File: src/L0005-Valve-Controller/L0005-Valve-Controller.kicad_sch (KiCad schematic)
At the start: 62 parts, among them J1 Jumper_NO, J2 Jumper_NO, P1 3220-20-0200-00, P10 353620650, P11 353620650, P12 353620650, P13 353620650, P14 647676-3, P15 647676-3, P16 647676-2, P2 140-504-415-000, P9 647676-2, U1 LPC54113J256BD64QL, U2 LMS8117AMP-3.3_NOPB, U3 MAX3370EXK+T, U4 MAX3370EXK+T, U5 Optocoupler

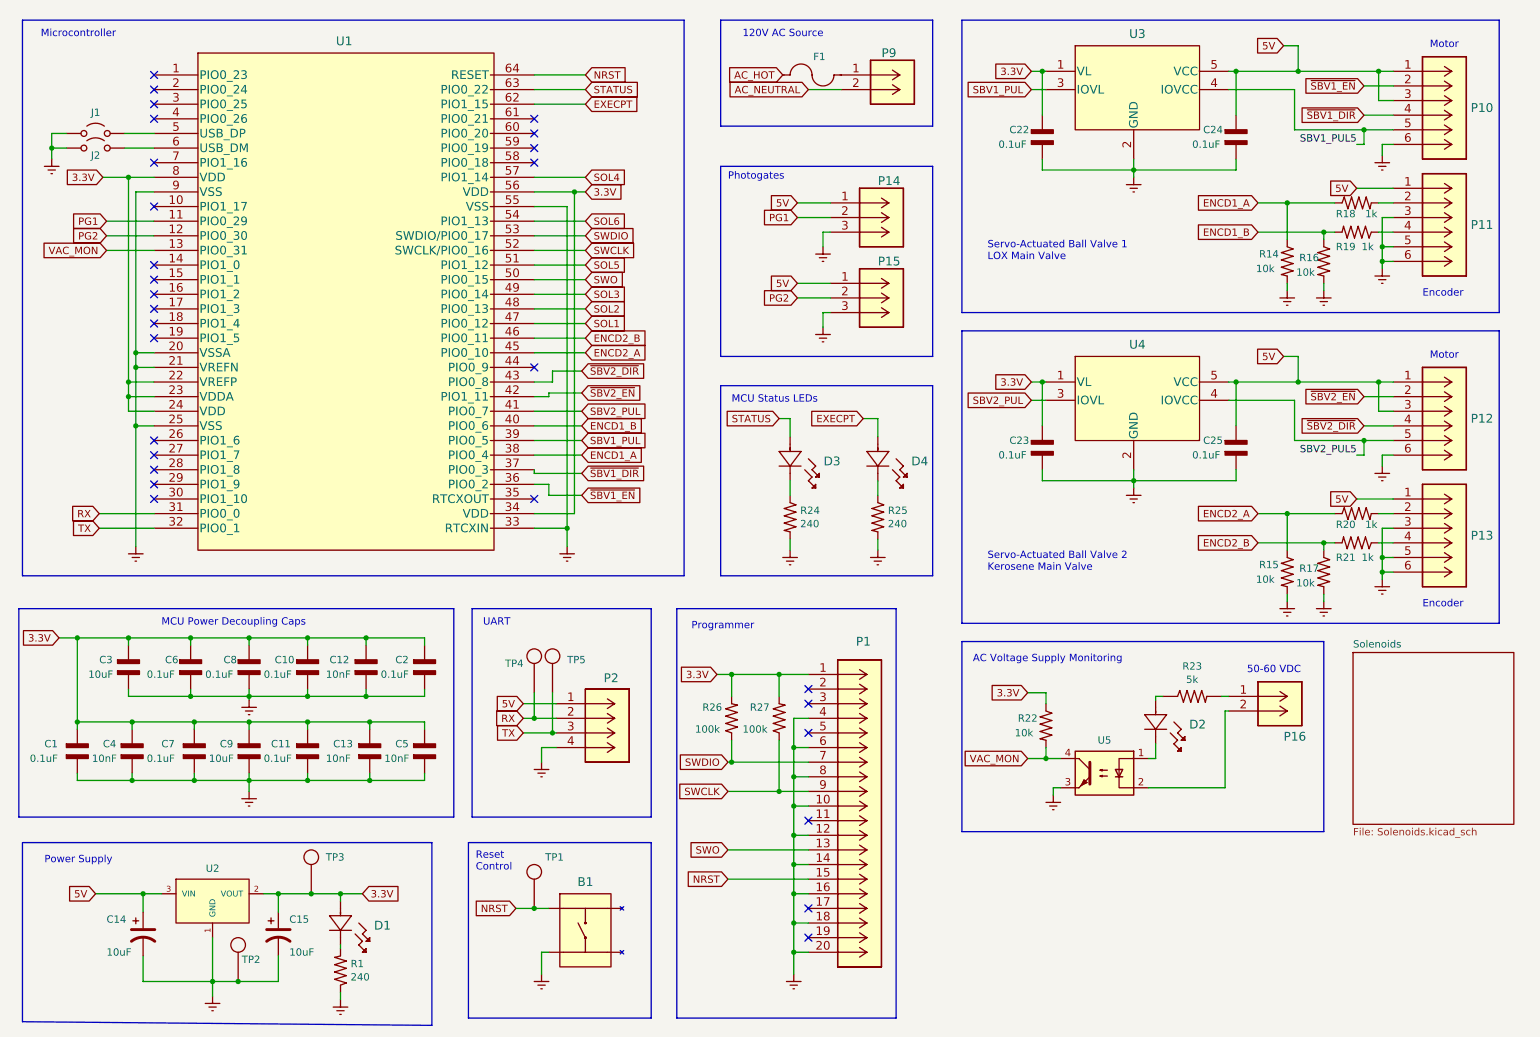
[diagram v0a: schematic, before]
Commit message: moved stepper circuits to second schematic sheet
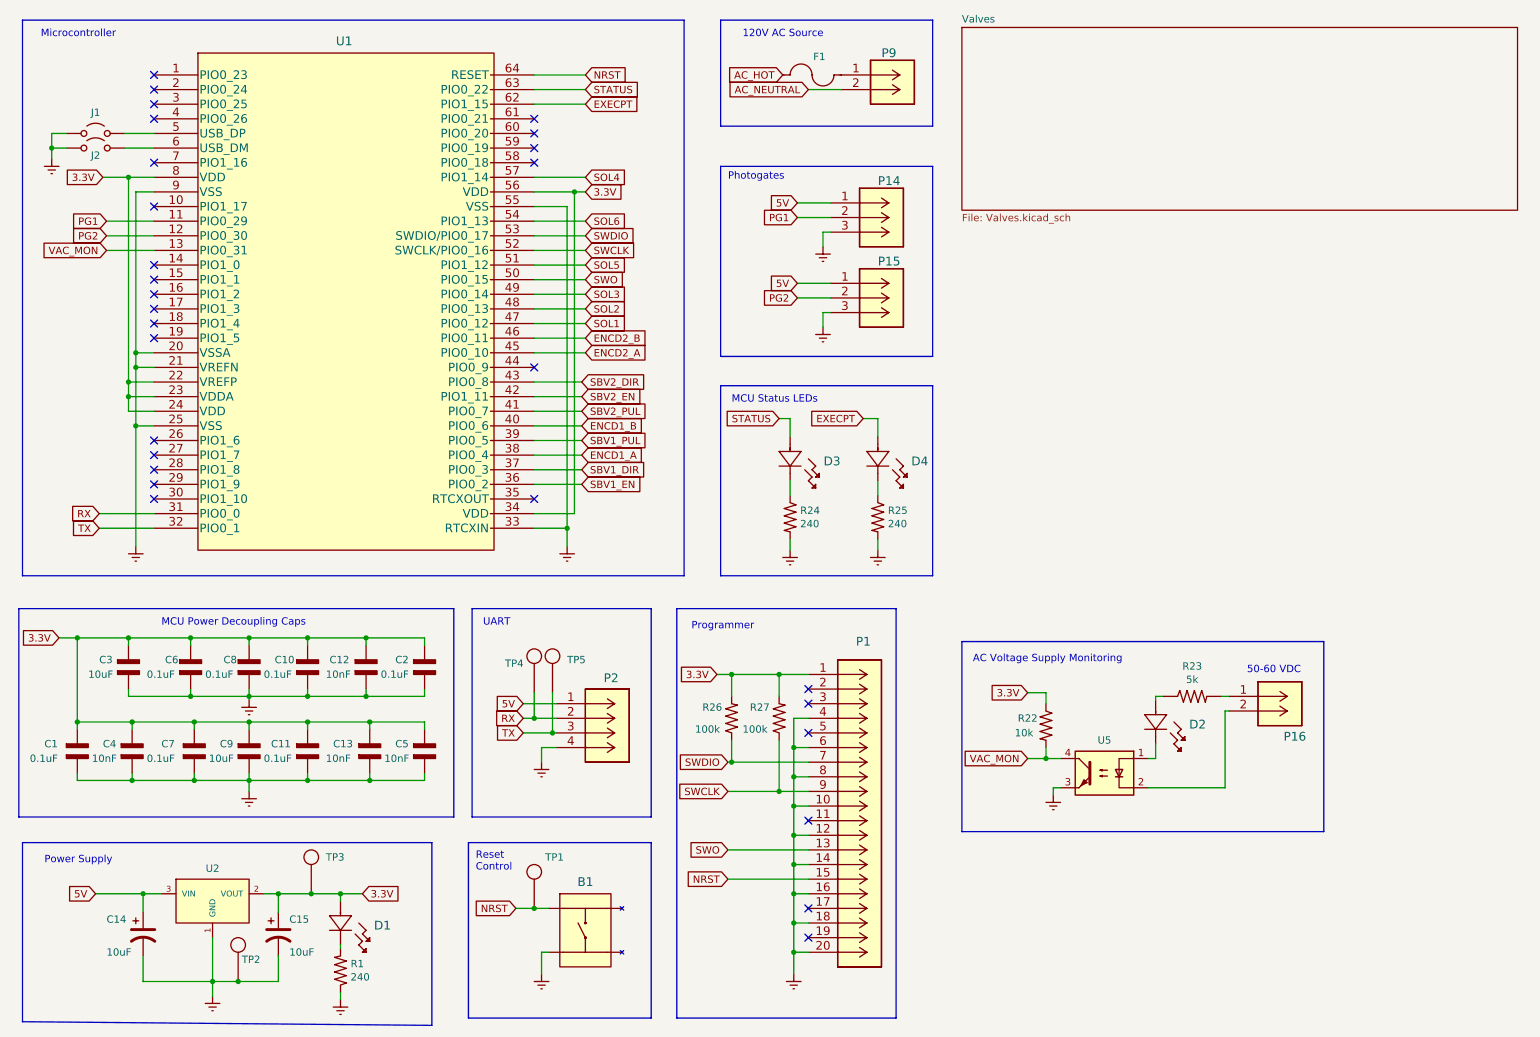
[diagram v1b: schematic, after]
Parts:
- removed C22, C23, C24, C25: 0.1uF, L0005-Valve-Controller:CAP_0603, symbol L0005-Valve-Controller:CAP_0603
- removed P10, P11, P12, P13: 353620650, L0005-Valve-Controller:MOLEX_35362-0650, symbol L0005-Valve-Controller:353620650
- removed R14, R15, R16, R17: 10k, L0005-Valve-Controller:RES_0603, symbol L0005-Valve-Controller:RES_0603
- removed R18, R19, R20, R21: 1k, L0005-Valve-Controller:RES_0603, symbol L0005-Valve-Controller:RES_0603
- removed U3, U4: MAX3370EXK+T, L0005-Valve-Controller:MAX3370EXK&plus_T, symbol L0005-Valve-Controller:MAX3370EXK+T
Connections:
- net ~{SBV1_DIR} renamed SBV1_DIR
- net ~{SBV1_EN} renamed SBV1_EN
- net ~{SBV2_DIR} renamed SBV2_DIR
- net ~{SBV2_EN} renamed SBV2_EN
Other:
- sheet Solenoids renamed Valves
- sheet Valves: file Solenoids.kicad_sch -> Valves.kicad_sch
- note removed: "Encoder"
- note removed: "Motor"
- note removed: "Servo-Actuated Ball Valve 1 LOX Main Valve"
- note removed: "Servo-Actuated Ball Valve 2 Kerosene Main Valve"

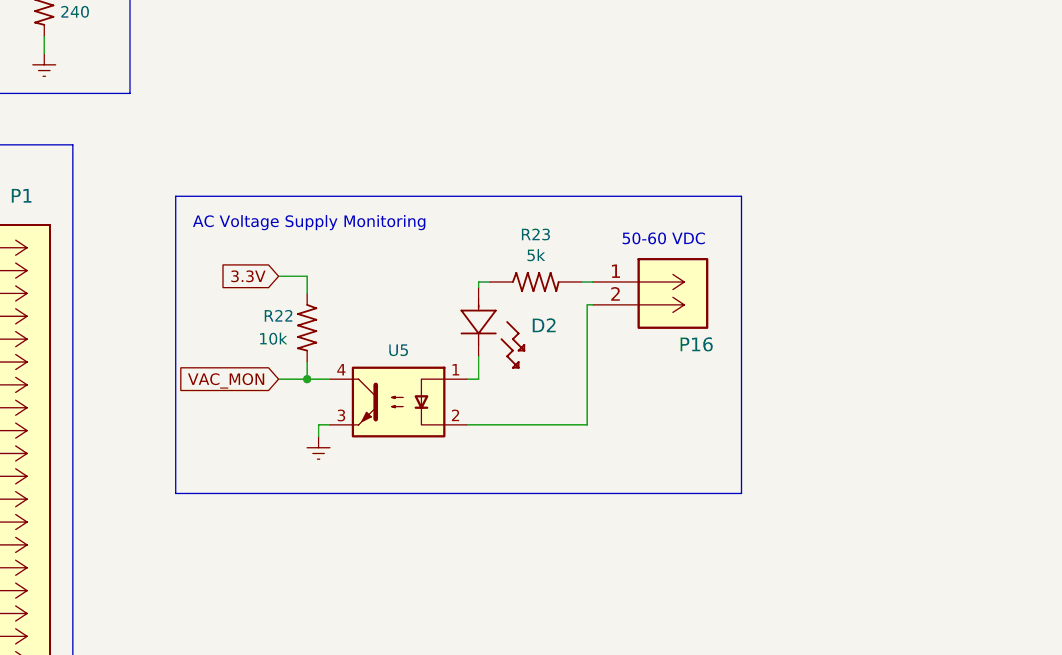
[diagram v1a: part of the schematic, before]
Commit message: inverted VAC_MON signal
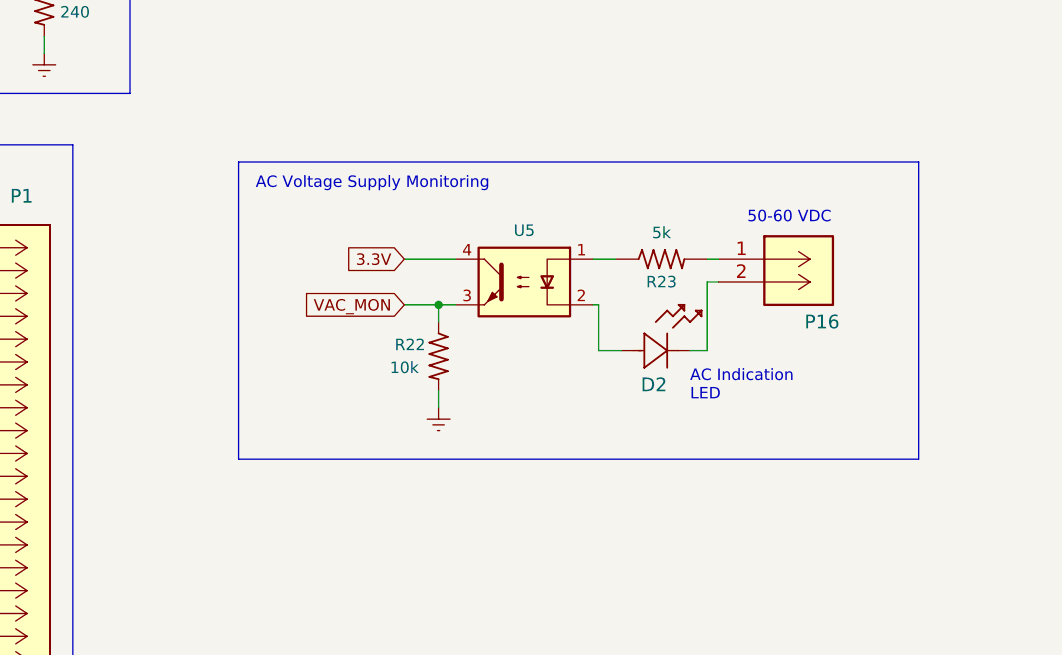
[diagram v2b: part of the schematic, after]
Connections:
- net 3.3V: now also U5.4; no longer R22.1
- net Earth: now also R22.2; no longer U5.3
- net VAC_MON: now also R22.1, U5.3; no longer R22.2, U5.4
- net at P16.2: now also D2.1; no longer U5.2
- net at U5.1: now also R23.1; no longer D2.1
- net at D2.2: now also U5.2; no longer R23.1
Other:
- note added: "AC Indication LED"
- moved on the sheet: D2, P16, R22, R23, U5

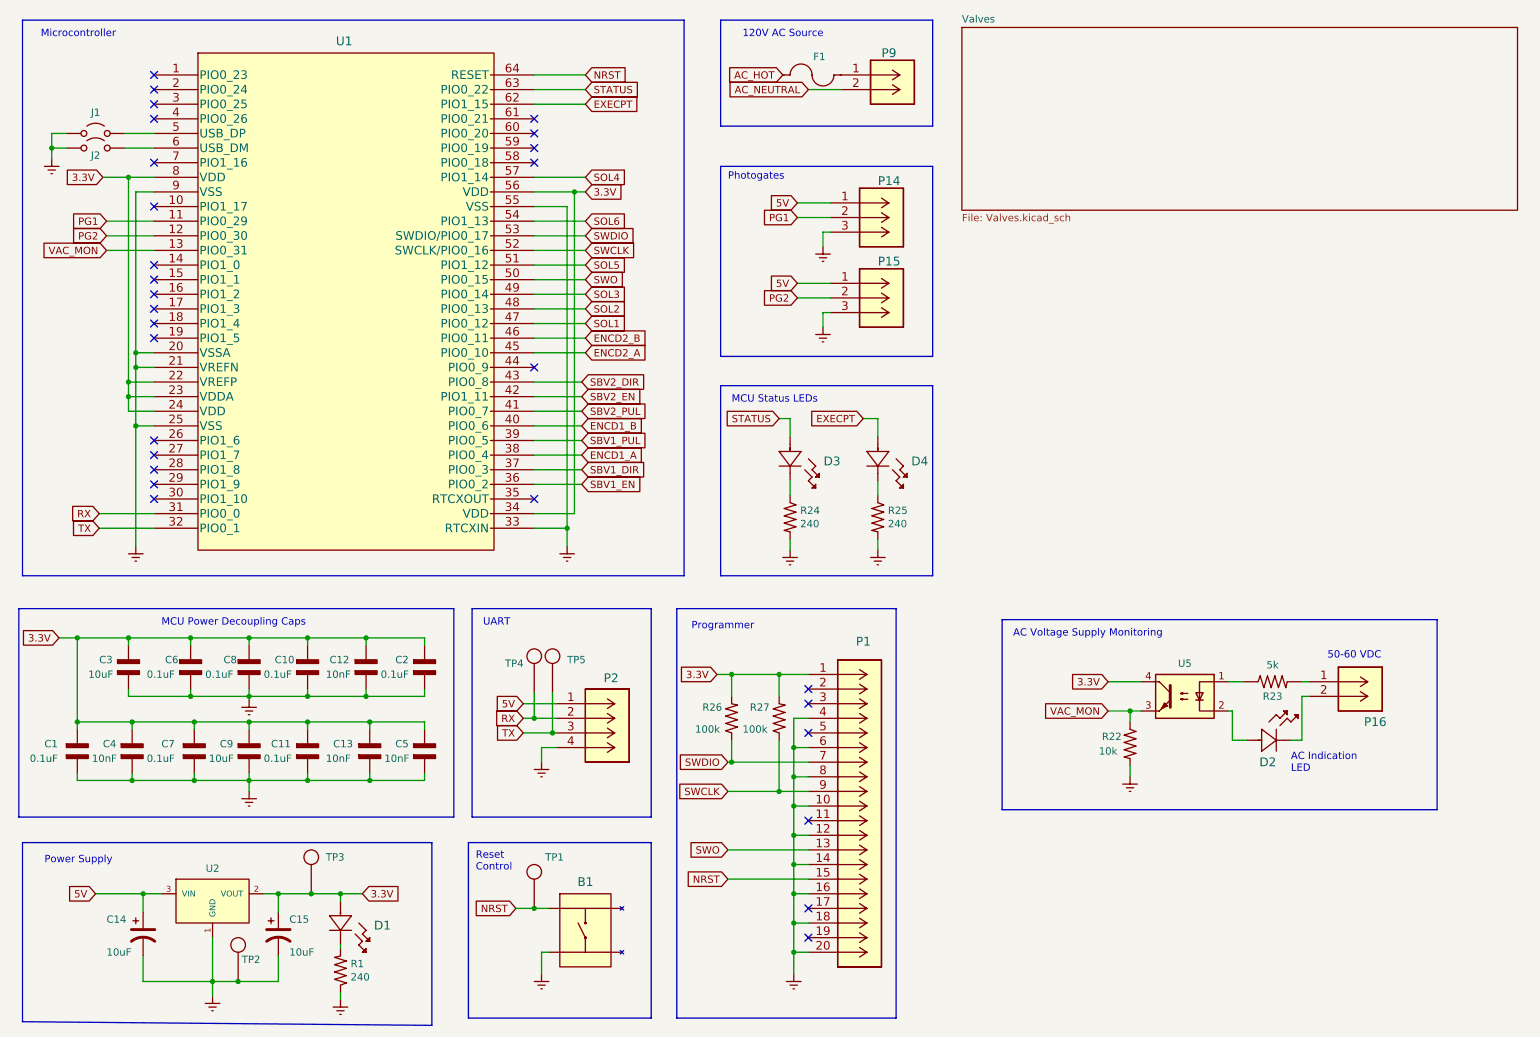
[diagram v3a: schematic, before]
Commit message: Rearranged schematic
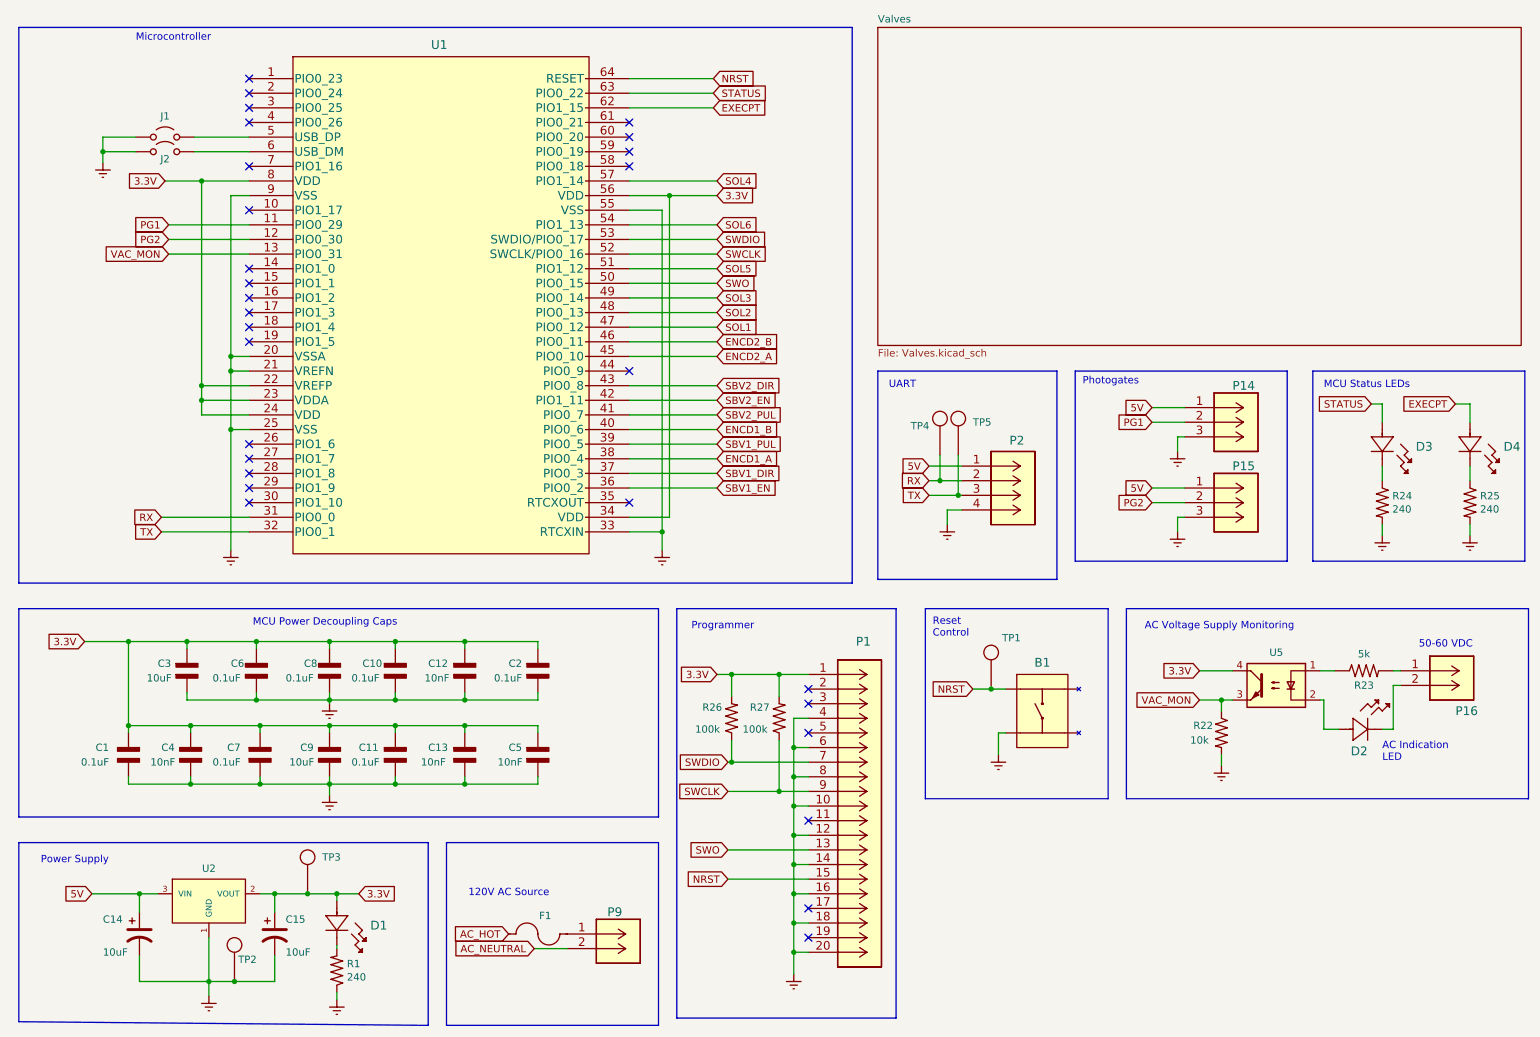
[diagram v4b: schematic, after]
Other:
- moved on the sheet: B1, C1, C10, C11, C12, C13, C14, C15, C2, C3, C4, C5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
